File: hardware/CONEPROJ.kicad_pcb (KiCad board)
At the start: 4 copper layers, 170.4 x 80 mm, 131 parts, among them J2 693071020811, J301 PWR-CAN, J302 LIPO, J304 U.FL-R-SMT-1(10), J305 GPS_MAG, J306 RGB OUT, J309 USB_B, J311 TC2030-IDC, J312 Conn_01x04, Q1 Q_NMOS_SGD, Q301 BSS138, Q302 BSS138, Q303 BSS138, U2 SN65HVD230, U3 PCA9685PW, U301 BQ29716DSET, U302 MP2615, U303 BQ29209DRBR, U304 AP1509, U306 MPU-9250, U307 ATECC608A-MAHDA-T, U308 BMP280, U310 RFM69HCW, U311 SN74LVC2G126DCUR, U4 TPD4S012DRYR, U5 MCP2515-xST, U6 RT9742GGJ5, U7 Pico, U8 MCP2515-xSO, Y2 16mhz

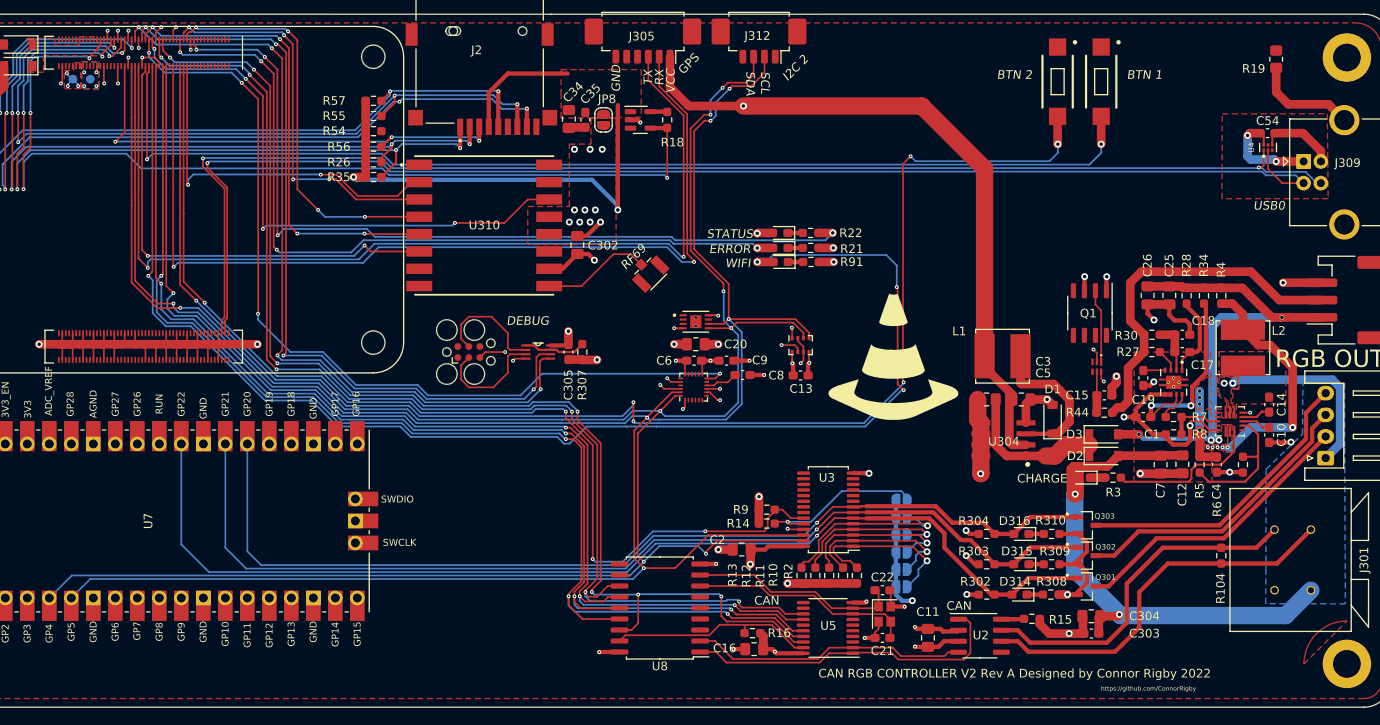
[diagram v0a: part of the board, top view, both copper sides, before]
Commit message: Remove BSS1338
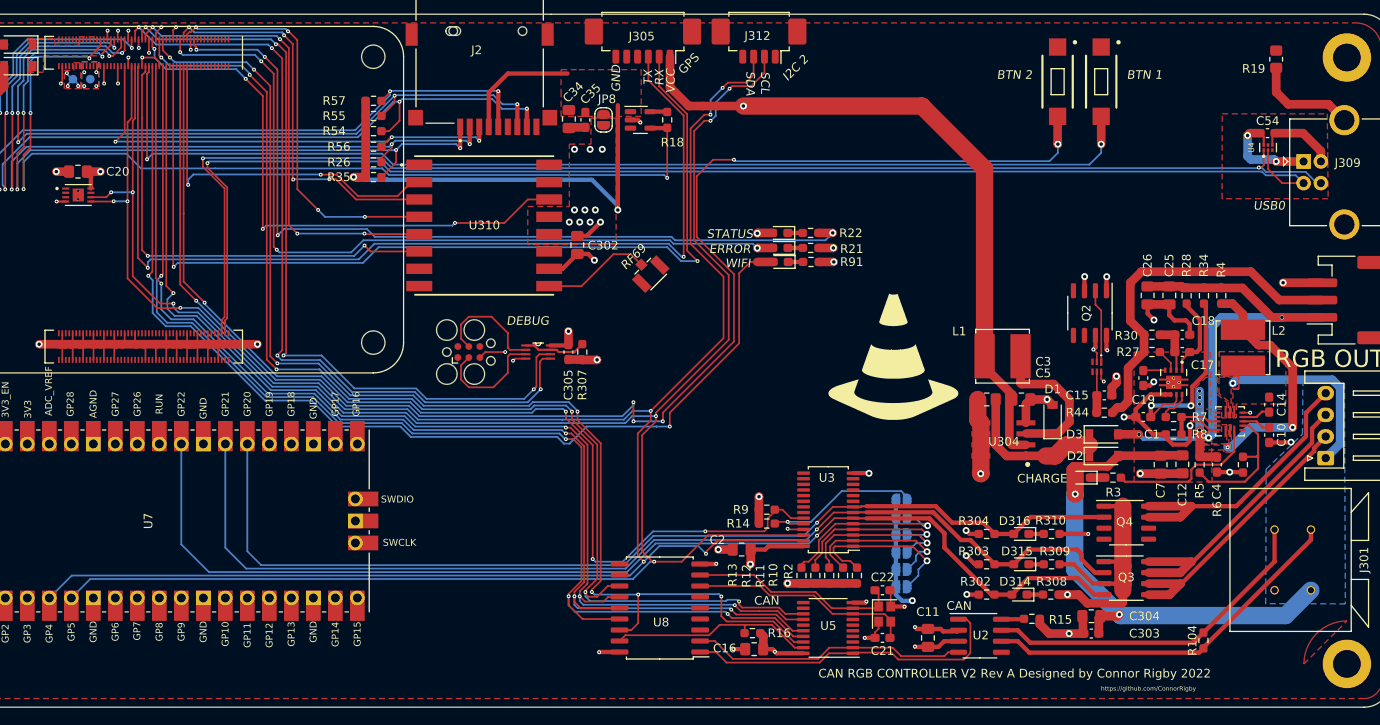
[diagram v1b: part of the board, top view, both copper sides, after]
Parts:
- removed C13, C6, C8, C9: 0.1uF, Capacitor_SMD:C_0603_1608Metric_Pad1.08x0.95mm_HandSolder
- removed Q1: Q_NMOS_SGD, Package_SO:SO-8_3.9x4.9mm_P1.27mm
- removed Q301, Q302, Q303: BSS138, SOT95P240X111-3N:SOT95P240X111-3N
- removed U306: MPU-9250, Sensor_Motion:InvenSense_QFN-24_3x3mm_P0.4mm
- removed U308: BMP280, Package_LGA:Bosch_LGA-8_2x2.5mm_P0.65mm_ClockwisePinNumbering
- added Q2: Q_Dual_NMOS_S1G1S2G2D2D2D1D1, Package_SO:SO-8_3.9x4.9mm_P1.27mm, F.Cu at (155.7, 54.5)
- added Q3: Q_Dual_NMOS_S1G1S2G2D2D2D1D1, Package_SO:SO-8_3.9x4.9mm_P1.27mm, F.Cu at (159.9, 85.1)
- added Q4: Q_Dual_NMOS_S1G1S2G2D2D2D1D1, Package_SO:SO-8_3.9x4.9mm_P1.27mm, F.Cu at (159.9, 78.7)
- moved C20 74.1 mm to (38.9, 38.2)
- moved U307 72.8 mm to (38.9, 40.9)
- moved R104 10.0 mm to (168.8, 92.3)
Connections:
- Module2 pad 47: /IMU_INT -> unconnected-(Module2-Pad47)
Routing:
- net /IMU_INT: track 101.9 -> 0.00 mm, vias 4 -> 0
- net /WIFI_LED: track 157.9 -> 121.2 mm, vias 4 -> 2
- net /I2C1_SCL: track 274.8 -> 254.9 mm, vias 6 -> 7
- net /I2C1_SDA: track 274.7 -> 256.1 mm
- net +3V3: track 69.9 -> 56.0 mm, vias 29 -> 22
- net GND: track 278.4 -> 284.8 mm, vias 64 -> 57
- net /SD_DAT1: track 98.4 -> 103.2 mm
- net /LED1: track 117.4 -> 121.8 mm
- net /LED0: track 124.4 -> 128.2 mm
- net Net-(C8-Pad1): track 3.78 -> 0.00 mm
- net /LED2: track 113.9 -> 116.9 mm
- net /MODE_BTN: track 168.5 -> 171.0 mm
- net /G_OUT: track 33.7 -> 31.9 mm
- net /B_OUT: track 34.6 -> 32.9 mm
- net unconnected-(Q2-Pad3): track 0.00 -> 1.65 mm, vias 0 -> 1
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
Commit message: asdf
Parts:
- removed C1, C14, C15, C17, C18, C19: 0.1uF, Capacitor_SMD:C_0603_1608Metric_Pad1.08x0.95mm_HandSolder
- removed C10: 1uF, Capacitor_SMD:C_0603_1608Metric_Pad1.08x0.95mm_HandSolder
- removed C12, C25, C26, C7: 10uF, Capacitor_SMD:C_0805_2012Metric_Pad1.18x1.45mm_HandSolder
- removed D3: D_Small, Diode_SMD:D_SOD-123
- removed D305: GRN, LED_SMD:LED_0603_1608Metric_Pad1.05x0.95mm_HandSolder
- removed J302: LIPO, Connector_JST:JST_PH_S3B-PH-SM4-TB_1x03-1MP_P2.00mm_Horizontal
- removed L2: 6.8uH, Inductor_SMD:L_Bourns_SRN6045TA
- removed Q2: Q_Dual_NMOS_S1G1S2G2D2D2D1D1, Package_SO:SO-8_3.9x4.9mm_P1.27mm
- removed R27, R28, R34: 150, Resistor_SMD:R_0603_1608Metric_Pad0.98x0.95mm_HandSolder
- removed R3, R44: 1k, Resistor_SMD:R_0603_1608Metric_Pad0.98x0.95mm_HandSolder
- removed R30: 240, Resistor_SMD:R_0603_1608Metric_Pad0.98x0.95mm_HandSolder
- removed R4: 0.1k, Resistor_SMD:R_0603_1608Metric_Pad0.98x0.95mm_HandSolder
- removed R5, R6, R8: 10k, Resistor_SMD:R_0603_1608Metric_Pad0.98x0.95mm_HandSolder
- removed R7: 4.7k, Resistor_SMD:R_0603_1608Metric_Pad0.98x0.95mm_HandSolder
- removed U301: BQ29716DSET, BQ29716DSET:BQ29716DSET
- removed U302: MP2615, MP2615GQ-Z:MP2615GQ-Z
- removed U303: BQ29209DRBR, BQ29209DRBR:IC_DRV8601DRBT
- added J3: RGBA OUT, Connector_JST:JST_XH_S4B-XH-A_1x04_P2.50mm_Horizontal, F.Cu at (163.9, 57.5)
- added JP9: LEDA_BOUT, Jumper:SolderJumper-2_P1.3mm_Open_RoundedPad1.0x1.5mm, F.Cu at (157.8, 50.5)
- added U9: WS2815B, WS2815B:worldsemi-WS2815B-MFG, F.Cu at (152.1, 52.7)
- C4: value 1uF -> 0.1uF
- J305: value GPS_MAG -> GPS
- J312: value Conn_01x04 -> MAG
- moved C4 28.2 mm to (147.7, 55.2), turned to 180 degrees
- moved R19 27.9 mm to (156.9, 44.3), turned to 0 degrees
- moved R2 19.0 mm to (109.8, 84.8)
- moved C11 19.0 mm to (118.0, 92.0)
- moved C16 19.0 mm to (97.9, 93.3)
- moved C2 19.0 mm to (96.5, 81.8)
- moved C21 19.0 mm to (112.8, 92.0)
- moved C22 19.0 mm to (112.8, 86.5)
- moved C303 19.0 mm to (136.9, 91.5)
- moved C304 19.0 mm to (136.9, 89.5)
- moved C54 19.0 mm to (157.2, 33.7)
- moved D314 19.0 mm to (128.6, 87.0)
- moved D315 19.0 mm to (128.8, 83.5)
- moved D316 19.0 mm to (128.8, 80.0)
- moved H302 19.0 mm to (166.4, 25.0)
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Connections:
- net /VCC renamed VCC
- net Net-(C3-Pad1) renamed /VIN
- C4 pad 1: /VCC_CHG -> Net-(U9-Pad1)
- Q4 pad 5: unconnected-(Q4-Pad5) -> /SPARE_OUT
- Q4 pad 6: unconnected-(Q4-Pad6) -> /SPARE_OUT
- U7 pad 22: unconnected-(U7-Pad22) -> /LEDA_BIN
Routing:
- net /LEDA_BIN: track 0.00 -> 102.5 mm, vias 0 -> 3
- net GND: track 284.8 -> 220.0 mm, vias 57 -> 54
- net /V_BATT: track 54.4 -> 0.00 mm, vias 3 -> 0
- net /BATT_MID: track 41.5 -> 0.00 mm
- net /R_OUT: track 33.9 -> 0.00 mm
- net /B_OUT: track 32.9 -> 0.00 mm
- net /G_OUT: track 31.9 -> 0.00 mm
- net Net-(L2-Pad2): track 27.7 -> 0.00 mm, vias 2 -> 0
- net /MODE_BTN: track 171.0 -> 147.7 mm, vias 6 -> 4
- net Net-(C1-Pad1): track 23.0 -> 0.00 mm, vias 2 -> 0
- net /I2C1_SDA: track 256.1 -> 234.9 mm
- net /I2C1_SCL: track 254.9 -> 234.1 mm, vias 7 -> 8
- net /LED1: track 121.8 -> 102.0 mm
- net /PWM0_1: track 122.1 -> 102.4 mm
- net /VIN: track 19.6 -> 0.00 mm
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- added copper zone on F.Cu, net +5V
- added copper zone on F.Cu, net /B_OUT
- added copper zone on F.Cu, net /G_OUT
- added copper zone on F.Cu, net /R_OUT
- added copper zone on F.Cu, net /SPARE_OUT
- added copper zone on F.Cu, net /VIN
- added copper zone on F.Cu, net GNDPWR
- added copper zone on F.Cu, net Net-(D1-Pad1)
- removed copper zone on F.Cu, net /VCC_CHG
- removed copper zone on F.Cu, net /V_BATT
- removed copper zone on F.Cu, net Net-(C14-Pad1)
- removed copper zone on F.Cu, net Net-(L2-Pad2)
- removed copper zone on F.Cu, net VCC
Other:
- board size 170.4 x 80 mm -> 151.4 x 80 mm
- board text added: "+12v"
- board text added: "BLUE"
- board text added: "BOUT"
- board text added: "DOUT"
- board text added: "GREEN"
- board text added: "Module2A"
- board text added: "Module2B"
- board text added: "RED"
- board text added: "RGB"
- board text added: "RGBA"
- board text added: "USB"
- board text removed: "CHARGE"
- board text removed: "RGB OUT"
- board text removed: "USB0"

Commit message: i hate myself
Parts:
- removed C2: 10uF, Capacitor_SMD:C_0805_2012Metric_Pad1.18x1.45mm_HandSolder
- removed D314: GRN, LED_SMD:LED_0603_1608Metric_Pad1.05x0.95mm_HandSolder
- removed D315: RED, LED_SMD:LED_0603_1608Metric_Pad1.05x0.95mm_HandSolder
- removed D316: BLUE, LED_SMD:LED_0603_1608Metric_Pad1.05x0.95mm_HandSolder
- removed D6: D_Small, Diode_SMD:D_SOD-123
- removed J301: PWR-CAN, DT:DTM-13
- removed JP2: A0, Jumper:SolderJumper-2_P1.3mm_Open_RoundedPad1.0x1.5mm
- removed JP3: A1, Jumper:SolderJumper-2_P1.3mm_Open_RoundedPad1.0x1.5mm
- removed JP4: A2, Jumper:SolderJumper-2_P1.3mm_Open_RoundedPad1.0x1.5mm
- removed JP5: A3, Jumper:SolderJumper-2_P1.3mm_Open_RoundedPad1.0x1.5mm
- removed JP6: A4, Jumper:SolderJumper-2_P1.3mm_Open_RoundedPad1.0x1.5mm
- removed JP7: A5, Jumper:SolderJumper-2_P1.3mm_Open_RoundedPad1.0x1.5mm
- removed R11, R12, R2: 10k, Resistor_SMD:R_0603_1608Metric_Pad0.98x0.95mm_HandSolder
- removed R308, R309: 240, Resistor_SMD:R_0603_1608Metric_Pad0.98x0.95mm_HandSolder
- removed R310: 1k, Resistor_SMD:R_0603_1608Metric_Pad0.98x0.95mm_HandSolder
- removed U3: PCA9685PW, Package_SO:TSSOP-28_4.4x9.7mm_P0.65mm
- added C10: 0.1uF, Capacitor_SMD:C_0603_1608Metric_Pad1.08x0.95mm_HandSolder, F.Cu at (97.3, 69.8)
- added C12: 1uF, Capacitor_SMD:C_0603_1608Metric_Pad1.08x0.95mm_HandSolder, F.Cu at (103.8, 73.1)
- added C13: 0.1uF, Capacitor_SMD:C_0603_1608Metric_Pad1.08x0.95mm_HandSolder, F.Cu at (103.8, 76.5)
- added C14: 0.1uF, Capacitor_SMD:C_0603_1608Metric_Pad1.08x0.95mm_HandSolder, F.Cu at (103.8, 74.8)
- added C15: 0.1uF, Capacitor_SMD:C_0603_1608Metric_Pad1.08x0.95mm_HandSolder, F.Cu at (97.8, 85.2)
- added C17: 0.1uF, Capacitor_SMD:C_0603_1608Metric_Pad1.08x0.95mm_HandSolder, F.Cu at (87.3, 80.8)
- added C18: 0.1uF, Capacitor_SMD:C_0603_1608Metric_Pad1.08x0.95mm_HandSolder, F.Cu at (97.3, 71.4)
- added C19: 0.1uF, Capacitor_SMD:C_0603_1608Metric_Pad1.08x0.95mm_HandSolder, F.Cu at (89.0, 75.5)
- added C23: 0.1uF, Capacitor_SMD:C_0603_1608Metric_Pad1.08x0.95mm_HandSolder, F.Cu at (102.5, 79.7)
- added C24: 0.1uF, Capacitor_SMD:C_0603_1608Metric_Pad1.08x0.95mm_HandSolder, F.Cu at (108.3, 73.0)
- added C6: 1uF, Capacitor_SMD:C_0603_1608Metric_Pad1.08x0.95mm_HandSolder, F.Cu at (102.7, 62.5)
- added C7: 10pF, Capacitor_SMD:C_0603_1608Metric_Pad1.08x0.95mm_HandSolder, F.Cu at (91.0, 89.3)
- added C8: 10pF, Capacitor_SMD:C_0603_1608Metric_Pad1.08x0.95mm_HandSolder, F.Cu at (98.7, 89.3)
- added C9: 1uF, Capacitor_SMD:C_0603_1608Metric_Pad1.08x0.95mm_HandSolder, F.Cu at (97.8, 83.7)
- added J4: Conn_01x14, AT15:AT15-12PC, F.Cu at (55.0, 78.8)
- added J5: TC2030-IDC, Connector:Tag-Connect_TC2030-IDC-FP_2x03_P1.27mm_Vertical, F.Cu at (106.8, 57.0)
- added J6: Conn_01x14, AT15:AT15-12PC, F.Cu at (135.7, 78.8)
- added Q2: Q_Dual_NMOS_S1G1S2G2D2D2D1D1, Package_SO:SO-8_3.9x4.9mm_P1.27mm, F.Cu at (43.5, 67.5)
- added Q5: Q_Dual_NMOS_S1G1S2G2D2D2D1D1, Package_SO:SO-8_3.9x4.9mm_P1.27mm, F.Cu at (62.2, 67.4)
- added Q6: Q_Dual_NMOS_S1G1S2G2D2D2D1D1, Package_SO:SO-8_3.9x4.9mm_P1.27mm, F.Cu at (53.0, 67.5)
- added Q7: Q_Dual_NMOS_S1G1S2G2D2D2D1D1, Package_SO:SO-8_3.9x4.9mm_P1.27mm, F.Cu at (47.0, 90.0)
- added R23: 100k, Resistor_SMD:R_0603_1608Metric_Pad0.98x0.95mm_HandSolder, F.Cu at (51.5, 62.5)
- added R24: 100k, Resistor_SMD:R_0603_1608Metric_Pad0.98x0.95mm_HandSolder, F.Cu at (48.5, 97.0)
- added R27: 100k, Resistor_SMD:R_0603_1608Metric_Pad0.98x0.95mm_HandSolder, F.Cu at (48.5, 95.0)
- added R29: 100k, Resistor_SMD:R_0603_1608Metric_Pad0.98x0.95mm_HandSolder, F.Cu at (55.0, 62.5)
- added R3: 1k, Resistor_SMD:R_0603_1608Metric_Pad0.98x0.95mm_HandSolder, F.Cu at (89.1, 70.8)
- added R31: 100k, Resistor_SMD:R_0603_1608Metric_Pad0.98x0.95mm_HandSolder, F.Cu at (57.9, 97.0)
- added R4: 10k,DNF, Resistor_SMD:R_0603_1608Metric_Pad0.98x0.95mm_HandSolder, F.Cu at (90.7, 70.8)
- added R5: 1k, Resistor_SMD:R_0603_1608Metric_Pad0.98x0.95mm_HandSolder, F.Cu at (97.8, 86.8)
- added R6: 27.4, Capacitor_SMD:C_0603_1608Metric_Pad1.08x0.95mm_HandSolder, F.Cu at (103.8, 69.8)
- added R7: 27.4, Capacitor_SMD:C_0603_1608Metric_Pad1.08x0.95mm_HandSolder, F.Cu at (103.8, 71.5)
- added U10: RP2040, RP2040:RP2040-QFN-56, F.Cu at (95.5, 78.7)
- added Y3: 12mhz, Crystal:Crystal_SMD_3225-4Pin_3.2x2.5mm_HandSoldering, F.Cu at (94.9, 90.0)
- R10, R13, R14, R9: value 10k -> 100k
- U7: value Pico -> W25Q128JVS; footprint RP2040:RPi_Pico_SMD_TH -> Package_SO:SOIC-8_5.23x5.23mm_P1.27mm
- moved J306 87.6 mm to (78.5, 90.5), turned to 0 degrees
- moved Q3 85.5 mm to (55.5, 90.0), turned to 90 degrees
- moved G*** 79.6 mm to (108.0, -14.3)
- moved Q4 77.7 mm to (64.0, 90.0), turned to 90 degrees
- moved R303 67.8 mm to (57.9, 95.0), turned to 0 degrees
- moved J3 67.2 mm to (105.4, 90.6), turned to 0 degrees
- moved R13 63.0 mm to (44.5, 62.5), turned to 0 degrees
- moved R304 61.1 mm to (65.5, 95.0), turned to 0 degrees
- moved R9 60.7 mm to (40.5, 62.5), turned to 0 degrees
- moved R302 60.1 mm to (65.5, 97.0), turned to 0 degrees
- moved C16 58.9 mm to (134.8, 47.3)
- moved C21 58.9 mm to (149.6, 46.0)
- moved C22 58.9 mm to (149.6, 40.5)
- moved R16 58.9 mm to (134.6, 45.5)
- moved U8 58.9 mm to (123.9, 42.5)
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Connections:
- J306 pad 2: /G_OUT -> /R_OUT
- J306 pad 3: /R_OUT -> /G_OUT
- JP9 pad 1: /LEDA_BIN -> /LEDA
- Module2 pad 28: /PWM0_1 -> unconnected-(Module2-Pad28)
- Module2 pad 31: /PWM0_0 -> unconnected-(Module2-Pad31)
- Module2 pad 37: /SPI0_CE1_N -> unconnected-(Module2-Pad37)
- Q3 pad 2: /LED1 -> /GPO_9
- Q3 pad 4: /LED0 -> /LEDR
- Q3 pad 5: /G_OUT -> /R_OUT
- Q3 pad 6: /G_OUT -> /R_OUT
- Q3 pad 7: /R_OUT -> /GPO_9_OUT
- Q3 pad 8: /R_OUT -> /GPO_9_OUT
- Q4 pad 2: /LED2 -> /LEDG
- Q4 pad 3: unconnected-(Q4-Pad3) -> GND
- Q4 pad 4: unconnected-(Q4-Pad4) -> /LEDB
- Q4 pad 5: /SPARE_OUT -> /B_OUT
- Q4 pad 6: /SPARE_OUT -> /B_OUT
- Q4 pad 7: /B_OUT -> /G_OUT
- Q4 pad 8: /B_OUT -> /G_OUT
- R10 pad 1: /A1 -> /GPO_5
- R13 pad 1: /A4 -> /GPO_2
- R14 pad 1: /A5 -> /GPO_6
- R302 pad 1: /LED0 -> /LEDG
- R303 pad 1: /LED1 -> /LEDR
- R304 pad 1: /LED2 -> /LEDB
- R9 pad 1: /PWM0_1 -> /GPO_1
- U7 pad 1: unconnected-(U7-Pad1) -> /QSPI_SS
- U7 pad 2: unconnected-(U7-Pad2) -> /QSPI_SD1
- U7 pad 3: GND -> /QSPI_SD2
- U7 pad 4: unconnected-(U7-Pad4) -> GND
- U7 pad 5: unconnected-(U7-Pad5) -> /QSPI_SD0
- U7 pad 6: /I2C1_SDA -> /QSPI_SCLK
- U7 pad 7: /I2C1_SCL -> /QSPI_SD3
- U7 pad 8: GND -> +3V3
- U9 pad 4: /LEDA_BIN -> /LEDA
- U9 pad 6: /LEDA_BIN -> /LEDA
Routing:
- net /USB2_VBUS: track 158.0 -> 1.55 mm, vias 3 -> 0
- net /LED0: track 109.1 -> 0.00 mm, vias 1 -> 0
- net /LEDA_BIN: track 102.5 -> 0.00 mm, vias 3 -> 0
- net /PWM0_1: track 102.4 -> 0.00 mm, vias 4 -> 0
- net /LED1: track 102.0 -> 0.00 mm, vias 1 -> 0
- net /LED2: track 98.0 -> 0.00 mm, vias 1 -> 0
- net +5V: track 194.4 -> 111.8 mm
- net /GPO_1: track 0.00 -> 62.0 mm
- net /MCP_RESET: track 24.0 -> 82.8 mm, vias 0 -> 1
- net /GPO_2: track 0.00 -> 58.4 mm
- net /GPO_7: track 0.00 -> 56.8 mm
- net /GPO_8: track 0.00 -> 51.2 mm
- net unconnected-(U10-Pad29): track 0.00 -> 50.5 mm
- net /MODE_BTN: track 147.7 -> 97.7 mm, vias 4 -> 2
- net /GPO_3: track 0.00 -> 49.9 mm
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- added copper zone on F.Cu, net /GPO_1_OUT
- added copper zone on F.Cu, net /GPO_2_OUT
- removed copper zone on F.Cu, net /B_OUT
- removed copper zone on F.Cu, net /G_OUT
- removed copper zone on F.Cu, net /R_OUT
- removed copper zone on F.Cu, net /SPARE_OUT
- removed copper zone on B.Cu, net VCC
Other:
- board text removed: "USB"

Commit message: what am i even doing
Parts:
- removed C20: 10uF, Capacitor_SMD:C_0805_2012Metric_Pad1.18x1.45mm_HandSolder
- removed C54: 0.1uF, Capacitor_SMD:C_0603_1608Metric_Pad1.08x0.95mm_HandSolder
- removed H303: MountingHole_Pad, MountingHole:MountingHole_3.2mm_M3_DIN965_Pad
- removed J3: RGBA OUT, Connector_JST:JST_XH_S4B-XH-A_1x04_P2.50mm_Horizontal
- removed J305: GPS, Connector_Molex:Molex_PicoBlade_53261-0671_1x06-1MP_P1.25mm_Horizontal
- removed J309: USB_B, Connector_USB:USB_B_OST_USB-B1HSxx_Horizontal
- removed J312: MAG, Connector_Molex:Molex_PicoBlade_53261-0471_1x04-1MP_P1.25mm_Horizontal
- removed JP9: LEDA_BOUT, Jumper:SolderJumper-2_P1.3mm_Open_RoundedPad1.0x1.5mm
- removed R19: 0.1, Resistor_SMD:R_0805_2012Metric_Pad1.20x1.40mm_HandSolder
- removed U307: ATECC608A-MAHDA-T, SON50P200X300X60-9N:SON50P200X300X60-9N
- removed U4: TPD4S012DRYR, PSON50P145X100X60-6N:PSON50P145X100X60-6N
- added R2: R_Small, Resistor_SMD:R_0603_1608Metric_Pad0.98x0.95mm_HandSolder, F.Cu at (62.1, 128.7)
- added R8: R_Small, Resistor_SMD:R_0603_1608Metric_Pad0.98x0.95mm_HandSolder, F.Cu at (62.1, 130.2)
- J306: footprint Connector_JST:JST_XH_S4B-XH-A_1x04_P2.50mm_Horizontal -> Connector_JST:JST_XH_S5B-XH-A-1_1x05_P2.50mm_Horizontal
- J4: value Conn_01x14 -> DTM1312PA12PBR008; footprint AT15:AT15-12PC -> TE_DTM1312PA12PBR008:TE_DTM1312PA12PBR008
- J6: value Conn_01x14 -> UC-31PFFP-QS8001; footprint AT15:AT15-12PC -> AMPHENOL_UC-31PFFP-QS8001:AMPHENOL_UC-31PFFP-QS8001
- Q2, Q3, Q4, Q5, Q6, Q7, R10, R13, R14, R23, R24, R27, R29, R302, R303, R304, R31, R9: moved to B.Cu
- moved G*** 125.7 mm to (35.5, 88.2)
- moved R22 125.3 mm to (31.9, 116.5), turned to 180 degrees
- moved D1 125.0 mm to (25.4, 62.8), turned to -90 degrees
- moved R21 123.1 mm to (31.9, 115.0), turned to 180 degrees
- moved R91 121.0 mm to (31.9, 113.4), turned to 180 degrees
- moved D301 120.3 mm to (35.4, 116.5), turned to 0 degrees
- moved D302 118.0 mm to (35.4, 115.0), turned to 0 degrees
- moved C5 117.9 mm to (29.0, 65.1), turned to 180 degrees
- moved D2 117.6 mm to (29.5, 56.3), turned to 0 degrees
- moved D308 115.8 mm to (35.4, 113.4), turned to 0 degrees
- moved L1 114.4 mm to (31.7, 70.8), turned to 0 degrees
- moved J2 114.4 mm to (96.5, 135.8), turned to 0 degrees
- moved D5 113.8 mm to (82.0, 125.7), turned to -90 degrees
- moved U304 113.7 mm to (31.1, 60.5), turned to -90 degrees
- moved D4 112.6 mm to (84.3, 125.7), turned to -90 degrees
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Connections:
- J306 pad 2: /R_OUT -> /LEDA_OUT
- J306 pad 3: /G_OUT -> /R_OUT
- J306 pad 4: /B_OUT -> /G_OUT
- Q2 pad 2: /GPO_2 -> /GPO_9
- Q2 pad 4: /GPO_1 -> /LEDR
- Q2 pad 5: /GPO_1_OUT -> /R_OUT
- Q2 pad 6: /GPO_1_OUT -> /R_OUT
- Q2 pad 7: /GPO_2_OUT -> /GPO_9_OUT
- Q2 pad 8: /GPO_2_OUT -> /GPO_9_OUT
- Q3 pad 2: /GPO_9 -> /GPO_2
- Q3 pad 4: /LEDR -> /GPO_1
- Q3 pad 5: /R_OUT -> /GPO_1_OUT
- Q3 pad 6: /R_OUT -> /GPO_1_OUT
- Q3 pad 7: /GPO_9_OUT -> /GPO_2_OUT
- Q3 pad 8: /GPO_9_OUT -> /GPO_2_OUT
- Q4 pad 2: /LEDG -> /GPO_6
- Q4 pad 4: /LEDB -> /GPO_3
- Q4 pad 5: /B_OUT -> /GPO_3_OUT
- Q4 pad 6: /B_OUT -> /GPO_3_OUT
- Q4 pad 7: /G_OUT -> /GPO_6_OUT
- Q4 pad 8: /G_OUT -> /GPO_6_OUT
- Q5 pad 2: /GPO_6 -> /GPO_7
- Q5 pad 4: /GPO_5 -> /GPO_8
- Q5 pad 5: /GPO_5_OUT -> /GPO_8_OUT
- Q5 pad 6: /GPO_5_OUT -> /GPO_8_OUT
- Q5 pad 7: /GPO_6_OUT -> /GPO_7_OUT
- Q5 pad 8: /GPO_6_OUT -> /GPO_7_OUT
- Q6 pad 4: /GPO_3 -> /GPO_5
- Q6 pad 5: /GPO_3_OUT -> /GPO_5_OUT
- Q6 pad 6: /GPO_3_OUT -> /GPO_5_OUT
- Q7 pad 2: /GPO_7 -> /LEDG
- Q7 pad 4: /GPO_8 -> /LEDB
- Q7 pad 5: /GPO_8_OUT -> /B_OUT
- Q7 pad 6: /GPO_8_OUT -> /B_OUT
- Q7 pad 7: /GPO_7_OUT -> /G_OUT
- Q7 pad 8: /GPO_7_OUT -> /G_OUT
- R10 pad 1: /GPO_5 -> /GPO_8
- R13 pad 1: /GPO_2 -> /GPO_9
- R14 pad 1: /GPO_6 -> /GPO_7
- R23 pad 1: /GPO_3 -> /GPO_5
- R24 pad 1: /GPO_7 -> /LEDG
- R27 pad 1: /GPO_8 -> /LEDB
- R302 pad 1: /LEDG -> /GPO_6
- R303 pad 1: /LEDR -> /GPO_1
- R304 pad 1: /LEDB -> /GPO_3
- R31 pad 1: /GPO_9 -> /GPO_2
- R9 pad 1: /GPO_1 -> /LEDR
- U10 pad 11: /GPO_7 -> /GPO_4
- U10 pad 12: /GPO_8 -> /GPO_5
- U10 pad 13: /GPO_9 -> /GPO_6
- U10 pad 14: /LEDR -> /GPO_3
- U10 pad 15: /LEDG -> /GPO_2
- U10 pad 16: /LEDB -> /GPO_1
- U10 pad 17: unconnected-(U10-Pad17) -> /LEDA
- U10 pad 2: /GPO_6 -> /GPO_7
- U10 pad 28: /LEDA -> unconnected-(U10-Pad28)
- U10 pad 3: /GPO_5 -> /GPO_8
- U10 pad 4: /GPO_4 -> /GPO_9
- U10 pad 5: /GPO_3 -> /LEDR
- U10 pad 8: /GPO_2 -> /LEDG
- U10 pad 9: /GPO_1 -> /LEDB
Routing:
- net /I2C1_SCL: track 213.1 -> 107.6 mm, vias 5 -> 3
- net /I2C1_SDA: track 208.9 -> 107.4 mm, vias 5 -> 3
- net /SD_PWR_ON: track 112.6 -> 35.8 mm, vias 4 -> 2
- net /PAUSE_BTN: track 107.1 -> 32.8 mm
- net /SD_CLK: track 106.9 -> 35.2 mm, vias 5 -> 2
- net /SD_DAT1: track 103.2 -> 33.2 mm, vias 5 -> 2
- net /MCP_RESET: track 82.8 -> 20.5 mm, vias 1 -> 3
- net /GPO_1_OUT: track 0.00 -> 62.1 mm
- net /MODE_BTN: track 97.7 -> 36.5 mm
- net /GPO_2_OUT: track 0.00 -> 58.5 mm
- net /SD_DAT0: track 89.3 -> 33.0 mm, vias 5 -> 2
- net /LED_GRN: track 89.8 -> 34.8 mm
- net /SD_DAT3: track 92.2 -> 37.7 mm, vias 5 -> 2
- net /GPO_3_OUT: track 0.00 -> 54.4 mm
- net unconnected-(U10-Pad29): track 50.5 -> 0.00 mm
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- added copper zone on B.Cu, net +1V8
- added copper zone on B.Cu, net /B_OUT
- added copper zone on B.Cu, net /GPO_1_OUT
- added copper zone on B.Cu, net /GPO_2_OUT
- added copper zone on B.Cu, net /GPO_3_OUT
- added copper zone on B.Cu, net /GPO_4_OUT
- added copper zone on B.Cu, net /GPO_5_OUT
- added copper zone on B.Cu, net /GPO_6_OUT
- added copper zone on B.Cu, net /GPO_7_OUT
- added copper zone on B.Cu, net /GPO_8_OUT
- added copper zone on B.Cu, net /GPO_9_OUT
- added copper zone on B.Cu, net /G_OUT
- added copper zone on B.Cu, net /R_OUT
- removed copper zone on F.Cu, net /GPO_1_OUT
- removed copper zone on F.Cu, net /GPO_2_OUT
- removed copper zone on F.Cu, net /SD_PWR
- removed copper zone on F.Cu, net /USB2_VBUS
- removed copper zone on F.Cu, net GNDPWR
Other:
- board size 151.4 x 80 mm -> 86 x 100 mm
- board text removed: "+12v"
- board text removed: "BLUE"
- board text removed: "BLUE RED GREEN +12V"
- board text removed: "BOUT"
- board text removed: "BTN 1"
- board text removed: "BTN 2"
- board text removed: "CAN"
- board text removed: "DOUT"
- board text removed: "ERROR"
- board text removed: "GND"
- board text removed: "GND MID VBAT"
- board text removed: "GPS"
- board text removed: "GREEN"
- board text removed: "I2C 2"
- board text removed: "RED"
- board text removed: "RGB"
- board text removed: "RGBA"
- board text removed: "RX"
- board text removed: "SCL"
- board text removed: "SDA"
- board text removed: "STATUS"
- board text removed: "TX"
- board text removed: "VCC"
- board text removed: "WIFI"
